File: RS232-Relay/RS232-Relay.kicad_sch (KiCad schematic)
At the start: 47 parts, among them J1 Relay 1-4, J2 Conn_01x02, J3 Relay 5-8, J4 Conn_01x09, J5 Conn_01x09, J6 Relay 9-12, J7 RS232_1, J8 RS232_2, SW2 SW_SPST, SW3 SW_SPST, U1 TEC2-1210WI, U3 PCF8575DBR, U4 MAX3232

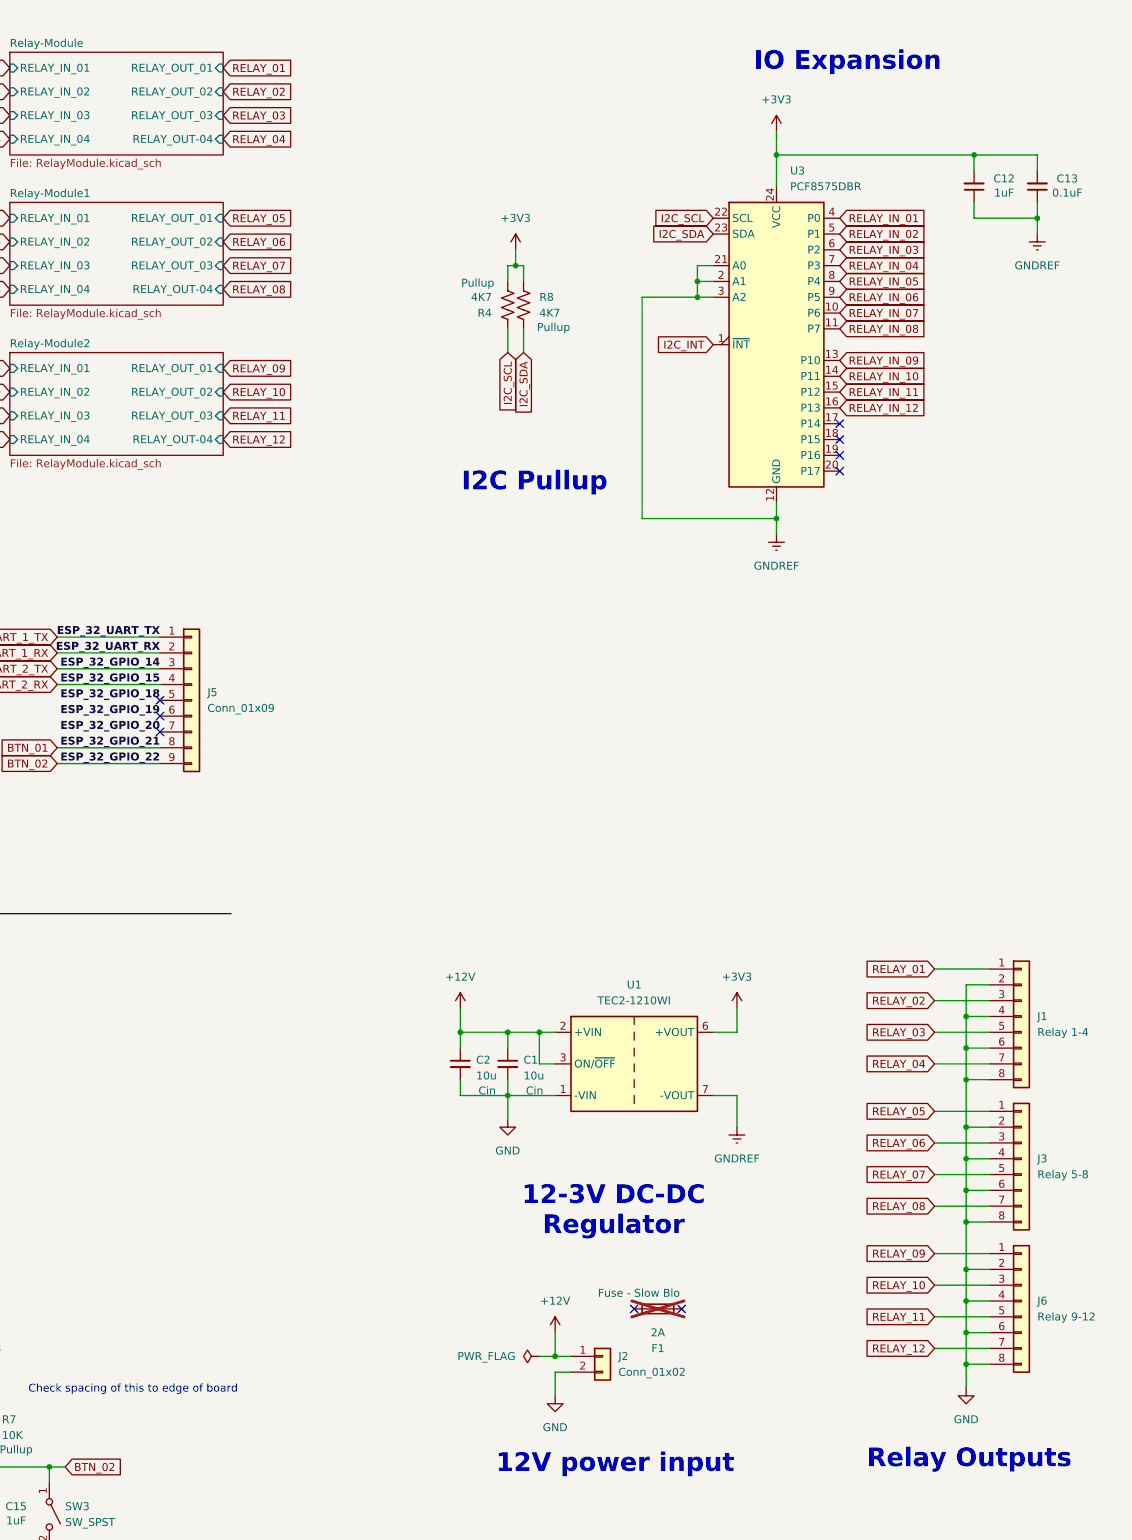
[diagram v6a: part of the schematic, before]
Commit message: Pre-template layouts
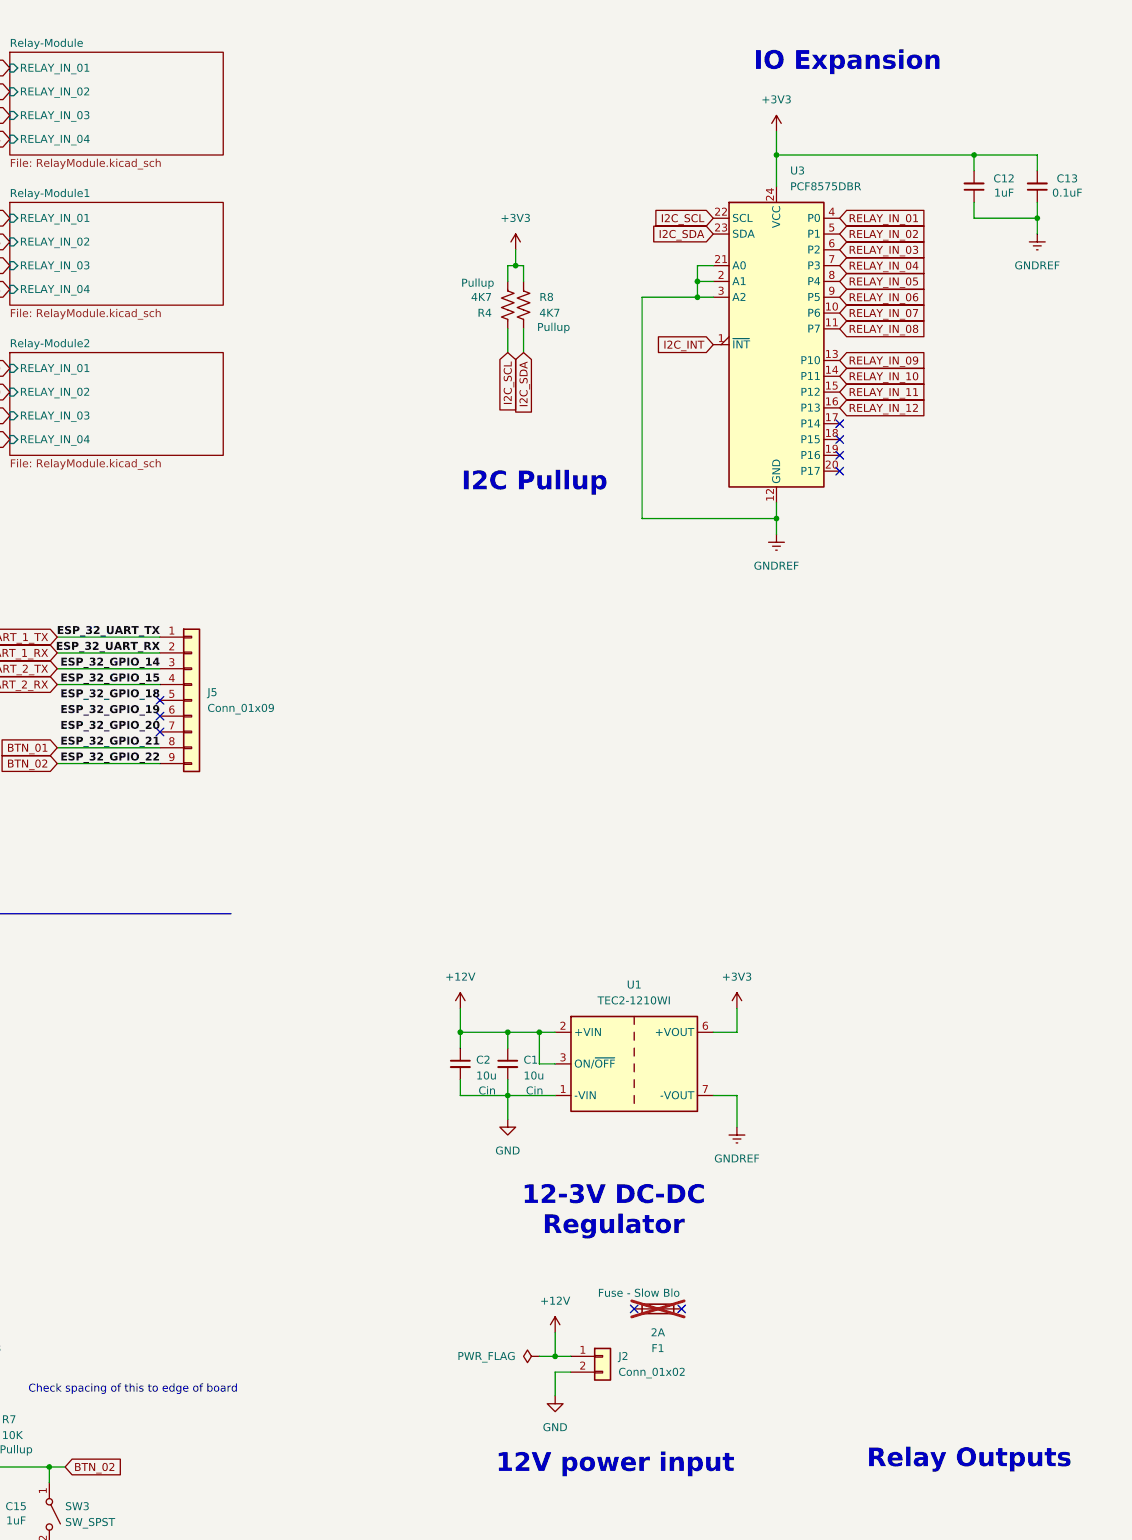
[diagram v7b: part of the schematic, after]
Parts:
- removed J1: Relay 1-4, Connector_Phoenix_MSTB:PhoenixContact_MSTBA_2,5_8-G-5,08_1x08_P5.08mm_Horizontal, symbol Connector_Generic:Conn_01x08
- removed J3: Relay 5-8, Connector_Phoenix_MSTB:PhoenixContact_MSTBA_2,5_8-G-5,08_1x08_P5.08mm_Horizontal, symbol Connector_Generic:Conn_01x08
- removed J6: Relay 9-12, Connector_Phoenix_MSTB:PhoenixContact_MSTBA_2,5_8-G-5,08_1x08_P5.08mm_Horizontal, symbol Connector_Generic:Conn_01x08
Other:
- sheet Relay-Module ports: added none; removed RELAY_OUT-04, RELAY_OUT_01, RELAY_OUT_02, RELAY_OUT_03
- sheet Relay-Module1 ports: added none; removed RELAY_OUT-04, RELAY_OUT_01, RELAY_OUT_02, RELAY_OUT_03
- sheet Relay-Module2 ports: added none; removed RELAY_OUT-04, RELAY_OUT_01, RELAY_OUT_02, RELAY_OUT_03

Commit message: Routing Complete (vias next)
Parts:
- removed D7: Green, LED_SMD:LED_0805_2012Metric, symbol Device:LED
- removed R9: 220R, Resistor_SMD:R_0603_1608Metric, symbol Device:R_US
- added C3: 10u, Capacitor_SMD:C_0603_1608Metric, symbol Device:C_Small
- added C4: 1uF, Capacitor_SMD:C_0402_1005Metric, symbol Device:C_Small
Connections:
- net +3V3: now also C3.1, C4.2
- net GNDREF: now also C3.2, C4.1
- net I2C_SCL: now also J4.7 (Pin_7); no longer J4.8 (Pin_8)
- net I2C_SDA: now also J4.8 (Pin_8); no longer J4.7 (Pin_7)
- net RELAY_IN_01: now also U3.16 (P13); no longer U3.4 (P0)
- net RELAY_IN_02: now also U3.15 (P12); no longer U3.5 (P1)
- net RELAY_IN_03: now also U3.14 (P11); no longer U3.6 (P2)
- net RELAY_IN_04: now also U3.13 (P10); no longer U3.7 (P3)
- net RELAY_IN_05: now also U3.11 (P7); no longer U3.8 (P4)
- net RELAY_IN_06: now also U3.10 (P6); no longer U3.9 (P5)
- net RELAY_IN_07: now also U3.9 (P5); no longer U3.10 (P6)
- net RELAY_IN_08: now also U3.8 (P4); no longer U3.11 (P7)
- net RELAY_IN_09: now also U3.7 (P3); no longer U3.13 (P10)
- net RELAY_IN_10: now also U3.6 (P2); no longer U3.14 (P11)
- net RELAY_IN_11: now also U3.5 (P1); no longer U3.15 (P12)
- net RELAY_IN_12: now also U3.4 (P0); no longer U3.16 (P13)
